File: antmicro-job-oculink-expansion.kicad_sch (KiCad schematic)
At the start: 21 parts, among them J1 OCuLink_x4_Amphenol_G14A42121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, J2 Plug_Samtec_ERM8_2x40_ERM8-04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, U1 MAX3373EEKA+

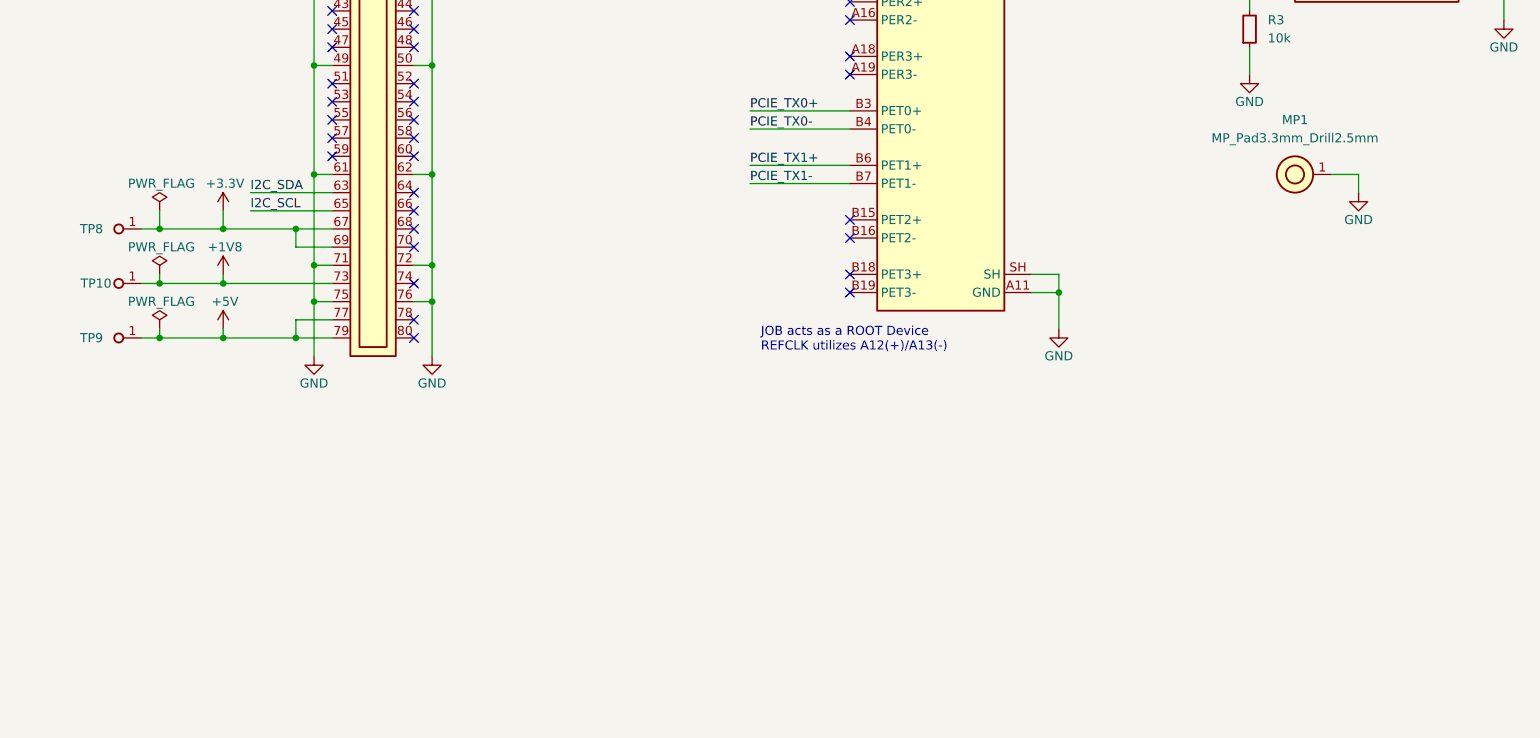
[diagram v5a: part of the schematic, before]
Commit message: [#74340] Update component placement
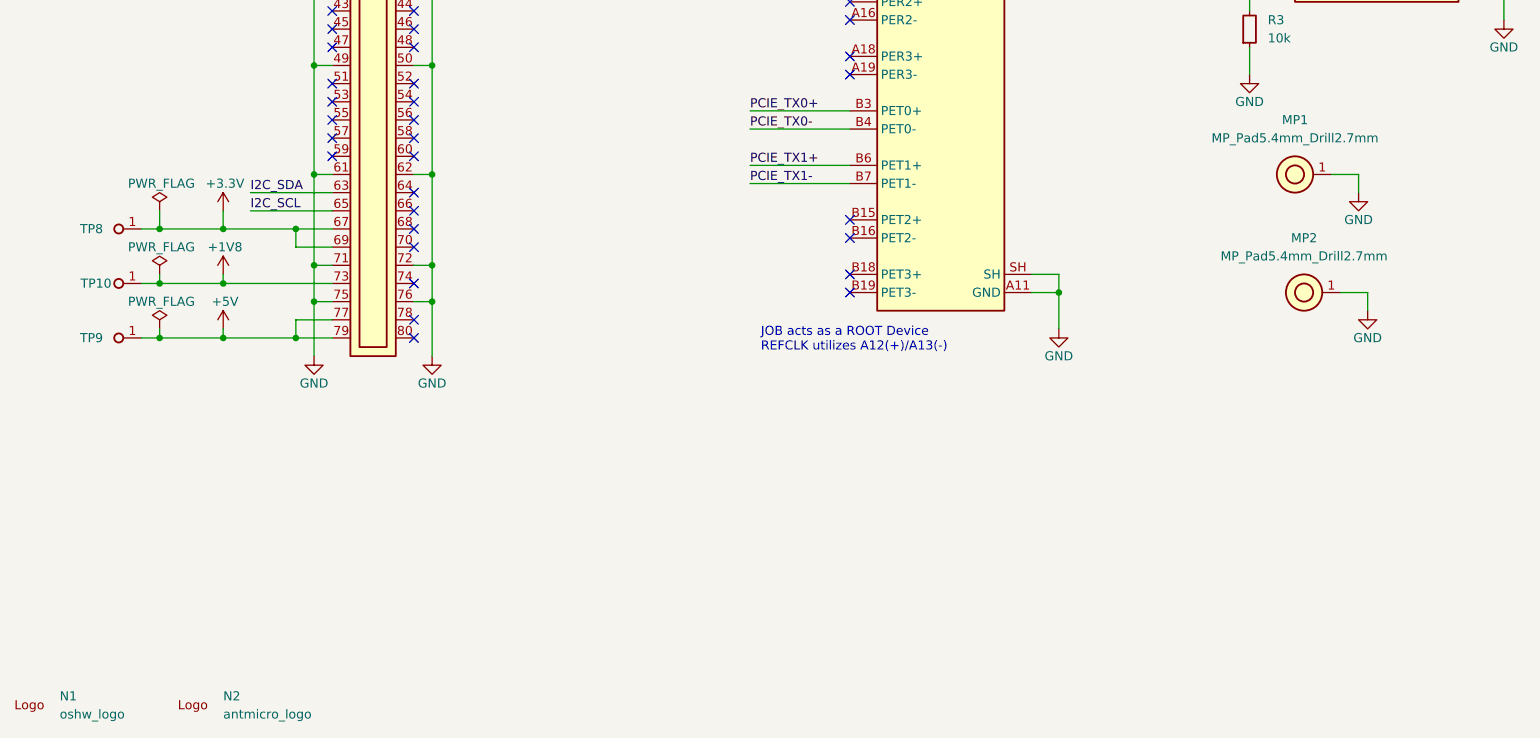
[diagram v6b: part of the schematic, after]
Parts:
- removed MP1: MP_Pad3.3mm_Drill2.5mm, antmicro-footprints:MP_Pad3.3mm_Drill2.5mm, symbol antmicroMechanicalParts:MP_Pad3.3mm_Drill2.5mm
- added MP1, MP2: MP_Pad5.4mm_Drill2.7mm, antmicro-footprints:MP_Pad5.4mm_Drill2.7mm, symbol antmicroMechanicalParts:MP_Pad5.4mm_Drill2.7mm
- added N1: oshw_logo, antmicro-footprints:oshw-logo, symbol antmicroMechanicalParts:oshw_logo
- added N2: antmicro_logo, antmicro-footprints:antmicro-logo_scaled_15mm, symbol antmicroMechanicalParts:antmicro_logo
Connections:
- net GND: now also MP1.1, MP2.1

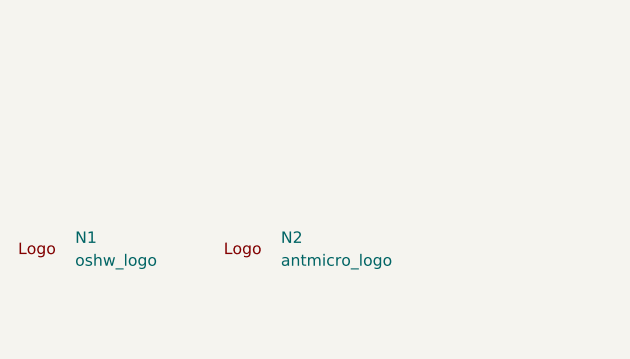
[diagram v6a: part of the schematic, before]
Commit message: [#74340] Add minor power plane adjustments
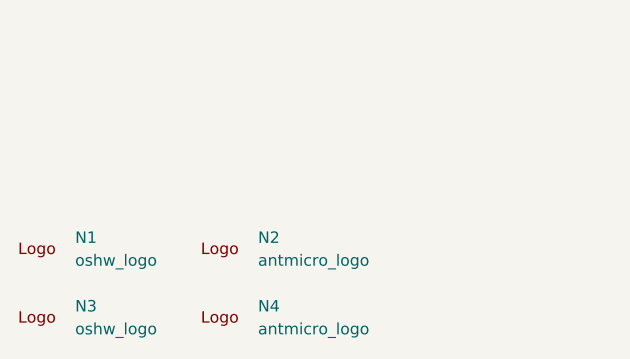
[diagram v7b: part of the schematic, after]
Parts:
- added N3: oshw_logo, antmicro-footprints:oshw-logo, symbol antmicroMechanicalParts:oshw_logo
- added N4: antmicro_logo, antmicro-footprints:antmicro-logo_scaled_15mm, symbol antmicroMechanicalParts:antmicro_logo
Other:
- moved on the sheet: N2
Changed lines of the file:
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@@
 	(symbol
 		(lib_id "antmicroMechanicalParts:antmicro_logo")
-		(at 48.26 185.42 0)
+		(at 45.72 185.42 0)
 		(unit 1)
 		(exclude_from_sim no)
@@
 		(fields_autoplaced yes)
 		(property "Reference" "N2"
-			(at 54.61 183.4362 0)
+			(at 52.07 183.4362 0)
 			(effects
 				(font
@@
 		)
 		(property "Value" "antmicro_logo"
-			(at 54.61 185.9762 0)
+			(at 52.07 185.9762 0)
 			(effects
 				(font
@@
 		)
 		(property "Footprint" "antmicro-footprints:antmicro-logo_scaled_15mm"
-			(at 63.5 195.58 0)
+			(at 60.96 195.58 0)
 			(effects
 				(font
@@
 		)
 		(property "Datasheet" ""
-			(at 63.5 198.12 0)
+			(at 60.96 198.12 0)
 			(effects
 				(font
@@
 		)
 		(property "Description" "Mechanical part"
-			(at 48.26 185.42 0)
+			(at 45.72 185.42 0)
 			(effects
 				(font
@@
 		)
 		(property "MPN" ""
-			(at 48.26 185.42 0)
+			(at 45.72 185.42 0)
 			(effects
 				(font
@@
 		)
 		(property "Manufacturer" ""
-			(at 63.5 205.74 0)
+			(at 60.96 205.74 0)
 			(effects
 				(font
@@
 		)
 		(property "Author" "Antmicro"
-			(at 63.5 200.66 0)
+			(at 60.96 200.66 0)
 			(effects
 				(font
@@
 		)
 		(property "License" "Apache-2.0"
-			(at 63.5 203.2 0)
+			(at 60.96 203.2 0)
 			(effects
 				(font
@@
 	)
 	(symbol
+		(lib_id "antmicroMechanicalParts:oshw_logo")
+		(at 25.4 193.04 0)
+		(unit 1)
+		(exclude_from_sim no)
+		(in_bom no)
+		(on_board yes)
+		(dnp no)
+		(fields_autoplaced yes)
+		(property "Reference" "N3"
+			(at 31.75 191.0562 0)
+			(effects
+				(font
+					(size 1.27 1.27)
+					(thickness 0.15)
+				)
+				(justify left)
+			)
+		)
+		(property "Value" "oshw_logo"
+			(at 31.75 193.5962 0)
+			(effects
+				(font
+					(size 1.27 1.27)
+					(thickness 0.15)
+				)
+				(justify left)
+			)
+		)
+		(property "Footprint" "antmicro-footprints:oshw-logo"
+			(at 40.64 203.2 0)
+			(effects
+				(font
+					(size 1.27 1.27)
+					(thickness 0.15)
+				)
+				(justify left bottom)
+				(hide yes)
+			)
+		)
+		(property "Datasheet" ""
+			(at 40.64 205.74 0)
+			(effects
+				(font
+					(size 1.27 1.27)
+					(thickness 0.15)
+				)
+				(justify left bottom)
+				(hide yes)
+			)
+		)
+		(property "Description" "Mechanical part"
+			(at 25.4 193.04 0)
+			(effects
+				(font
+					(size 1.27 1.27)
+				)
+				(hide yes)
+			)
+		)
+		(property "Author" "Antmicro"
+			(at 40.64 208.28 0)
+			(effects
+				(font
+					(size 1.27 1.27)
+					(thickness 0.15)
+				)
+				(justify left bottom)
+				(hide yes)
+			)
+		)
+		(property "License" "Apache-2.0"
+			(at 40.64 210.82 0)
+			(effects
+				(font
+					(size 1.27 1.27)
+					(thickness 0.15)
+				)
+				(justify left bottom)
+				(hide yes)
+			)
+		)
+		(property "MPN" ""
+			(at 25.4 193.04 0)
+			(effects
+				(font
+					(size 1.27 1.27)
+				)
+			)
+		)
+		(property "Manufacturer" ""
+			(at 40.64 213.36 0)
+			(effects
+				(font
+					(size 1.27 1.27)
+					(thickness 0.15)
+				)
+				(justify left bottom)
+				(hide yes)
+			)
+		)
+		(instances
+			(project "antmicro-job-oculink-expansion"
+				(path "/195f80bc-f1ce-461e-9433-be011ba7464b"
+					(reference "N3")
+					(unit 1)
+				)
+			)
+		)
+	)
+	(symbol
 		(lib_id "antmicropower:GND")
 		(at 214.63 129.54 0)
@@
 					(unit 1)
 				)
+			)
+		)
+	)
+	(symbol
+		(lib_id "antmicroMechanicalParts:antmicro_logo")
+		(at 45.72 193.04 0)
+		(unit 1)
+		(exclude_from_sim no)
+		(in_bom no)
+		(on_board yes)
+		(dnp no)
+		(fields_autoplaced yes)
+		(property "Reference" "N4"
+			(at 52.07 191.0562 0)
+			(effects
+				(font
+					(size 1.27 1.27)
+					(thickness 0.15)
+				)
+				(justify left)
+			)
+		)
+		(property "Value" "antmicro_logo"
+			(at 52.07 193.5962 0)
+			(effects
+				(font
+					(size 1.27 1.27)
+					(thickness 0.15)
+				)
+				(justify left)
+			)
+		)
+		(property "Footprint" "antmicro-footprints:antmicro-logo_scaled_15mm"
+			(at 60.96 203.2 0)
+			(effects
+				(font
+					(size 1.27 1.27)
+					(thickness 0.15)
+				)
+				(justify left bottom)
+				(hide yes)
+			)
+		)
+		(property "Datasheet" ""
+			(at 60.96 205.74 0)
+			(effects
+				(font
+					(size 1.27 1.27)
+					(thickness 0.15)
+				)
+				(justify left bottom)
+				(hide yes)
+			)
+		)
+		(property "Description" "Mechanical part"
+			(at 45.72 193.04 0)
+			(effects
+				(font
+					(size 1.27 1.27)
+				)
+				(hide yes)
+			)
+		)
+		(property "MPN" ""
+			(at 45.72 193.04 0)
+			(effects
+				(font
+					(size 1.27 1.27)
+				)
+			)
+		)
+		(property "Manufacturer" ""
+			(at 60.96 213.36 0)
+			(effects
+				(font
+					(size 1.27 1.27)
+					(thickness 0.15)
+				)
+				(justify left bottom)
+				(hide yes)
+			)
+		)
+		(property "Author" "Antmicro"
+			(at 60.96 208.28 0)
+			(effects
+				(font
+					(size 1.27 1.27)
+					(thickness 0.15)
+				)
+				(justify left bottom)
+				(hide yes)
+			)
+		)
+		(property "License" "Apache-2.0"
+			(at 60.96 210.82 0)
+			(effects
+				(font
+					(size 1.27 1.27)
+					(thickness 0.15)
+				)
+				(justify left bottom)
+				(hide yes)
+			)
+		)
+		(instances
+			(project "antmicro-job-oculink-expansion"
+				(path "/195f80bc-f1ce-461e-9433-be011ba7464b"
+					(reference "N4")
+					(unit 1)
+				)
